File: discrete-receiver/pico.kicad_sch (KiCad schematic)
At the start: 49 parts, among them J4 Debug Pins, J8 Extra GPIO, U6 RP2350A, U7 W25Q128, X2 X322512MSB4SI

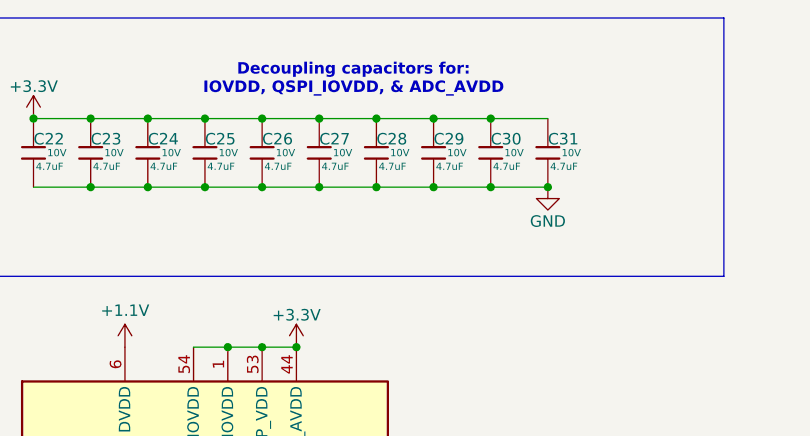
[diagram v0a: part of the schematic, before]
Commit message: Added test pads for SDA and SCL
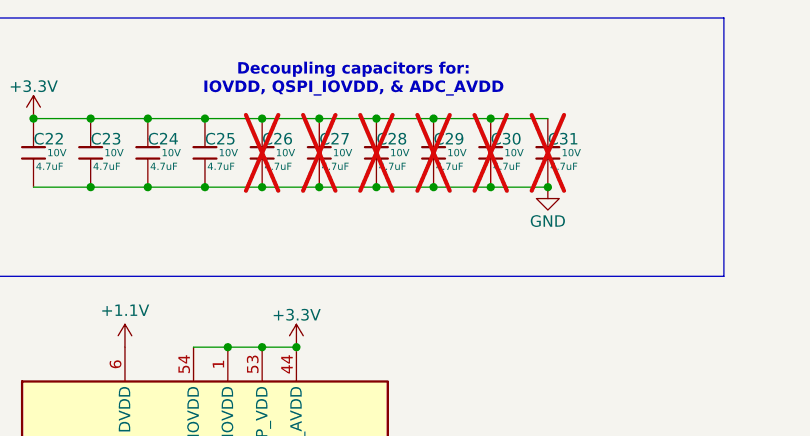
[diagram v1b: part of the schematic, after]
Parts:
- C26, C27, C28, C29, C30, C31: now not fitted; now left out of the parts list
- J8: footprint (none) -> Connector_PinHeader_2.54mm:PinHeader_1x05_P2.54mm_Vertical
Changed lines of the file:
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@@
 		(body_style 1)
 		(exclude_from_sim no)
-		(in_bom yes)
-		(on_board yes)
-		(in_pos_files yes)
-		(dnp no)
+		(in_bom no)
+		(on_board no)
+		(in_pos_files no)
+		(dnp yes)
 		(property "Reference" "C27"
 			(at 234.95 27.686 0)
@@
 		(body_style 1)
 		(exclude_from_sim no)
-		(in_bom yes)
-		(on_board yes)
-		(in_pos_files yes)
-		(dnp no)
+		(in_bom no)
+		(on_board no)
+		(in_pos_files no)
+		(dnp yes)
 		(property "Reference" "C28"
 			(at 241.3 27.686 0)
@@
 		(body_style 1)
 		(exclude_from_sim no)
-		(in_bom yes)
-		(on_board yes)
-		(in_pos_files yes)
-		(dnp no)
+		(in_bom no)
+		(on_board no)
+		(in_pos_files no)
+		(dnp yes)
 		(property "Reference" "C26"
 			(at 228.6 27.686 0)
@@
 			)
 		)
-		(property "Footprint" ""
+		(property "Footprint" "Connector_PinHeader_2.54mm:PinHeader_1x05_P2.54mm_Vertical"
 			(at 254 161.29 0)
 			(hide yes)
@@
 		(body_style 1)
 		(exclude_from_sim no)
-		(in_bom yes)
-		(on_board yes)
-		(in_pos_files yes)
-		(dnp no)
+		(in_bom no)
+		(on_board no)
+		(in_pos_files no)
+		(dnp yes)
 		(property "Reference" "C29"
 			(at 247.65 27.686 0)
@@
 		(body_style 1)
 		(exclude_from_sim no)
-		(in_bom yes)
-		(on_board yes)
-		(in_pos_files yes)
-		(dnp no)
+		(in_bom no)
+		(on_board no)
+		(in_pos_files no)
+		(dnp yes)
 		(property "Reference" "C30"
 			(at 254 27.686 0)
@@
 		(body_style 1)
 		(exclude_from_sim no)
-		(in_bom yes)
-		(on_board yes)
-		(in_pos_files yes)
-		(dnp no)
+		(in_bom no)
+		(on_board no)
+		(in_pos_files no)
+		(dnp yes)
 		(property "Reference" "C31"
 			(at 260.35 27.686 0)

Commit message: PCB Updates
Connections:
- net GND: now also J8.1 (Pin_1)
- net ~{ADC_RST}: now reaches U6.34 (GPIO22)
- net ~{ADC_RST}: no longer J8.1 (Pin_1)
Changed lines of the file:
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@@
 	(wire
 		(pts
+			(xy 259.08 153.67) (xy 259.08 156.21)
+		)
+		(stroke
+			(width 0)
+			(type default)
+		)
+	)
+	(wire
+		(pts
 			(xy 182.88 57.15) (xy 147.32 57.15)
 		)
@@
 	(wire
 		(pts
+			(xy 264.16 153.67) (xy 259.08 153.67)
+		)
+		(stroke
+			(width 0)
+			(type default)
+		)
+	)
+	(wire
+		(pts
 			(xy 147.32 52.07) (xy 147.32 57.15)
 		)
@@
 	(wire
 		(pts
-			(xy 259.08 156.21) (xy 259.08 130.81)
-		)
-		(stroke
-			(width 0)
-			(type default)
-		)
-	)
-	(wire
-		(pts
 			(xy 247.65 33.02) (xy 254 33.02)
 		)
@@
 	(wire
 		(pts
-			(xy 259.08 130.81) (xy 246.38 130.81)
-		)
-		(stroke
-			(width 0)
-			(type default)
-		)
-	)
-	(wire
-		(pts
 			(xy 147.32 52.07) (xy 147.32 49.53)
 		)
@@
 	(wire
 		(pts
+			(xy 264.16 156.21) (xy 264.16 153.67)
+		)
+		(stroke
+			(width 0)
+			(type default)
+		)
+	)
+	(wire
+		(pts
 			(xy 168.91 129.54) (xy 175.26 129.54)
 		)
@@
 		)
 	)
+	(hierarchical_label "~{ADC_RST}"
+		(shape input)
+		(at 246.38 130.81 0)
+		(effects
+			(font
+				(size 1.27 1.27)
+			)
+			(justify left)
+		)
+	)
 	(hierarchical_label "I2S_SCLK"
 		(shape input)
@@
 					(unit 1)
 				)
+			)
+		)
+	)
+	(symbol
+		(lib_id "power:GND")
+		(at 264.16 156.21 0)
+		(unit 1)
+		(body_style 1)
+		(exclude_from_sim no)
+		(in_bom yes)
+		(on_board yes)
+		(in_pos_files yes)
+		(dnp no)
+		(property "Reference" "#PWR020"
+			(at 264.16 162.56 0)
+			(hide yes)
+			(show_name no)
+			(do_not_autoplace no)
+			(effects
+				(font
+					(size 1.27 1.27)
+				)
+			)
+		)
+		(property "Value" "GND"
+			(at 264.16 159.766 0)
+			(show_name no)
+			(do_not_autoplace no)
+			(effects
+				(font
+					(size 1.27 1.27)
+				)
+			)
+		)
+		(property "Footprint" ""
+			(at 264.16 156.21 0)
+			(hide yes)
+			(show_name no)
+			(do_not_autoplace no)
+			(effects
+				(font
+					(size 1.27 1.27)
+				)
+			)
+		)
+		(property "Datasheet" ""
+			(at 264.16 156.21 0)
+			(hide yes)
+			(show_name no)
+			(do_not_autoplace no)
+			(effects
+				(font
+					(size 1.27 1.27)
+				)
+			)
+		)
+		(property "Description" "Power symbol creates a global label with name \"GND\" , ground"
+			(at 264.16 156.21 0)
+			(hide yes)
+			(show_name no)
+			(do_not_autoplace no)
+			(effects
+				(font
+					(size 1.27 1.27)
+				)
+			)
+		)
+		(pin "1"
+		)
+		(instances
+			(project "diode_tayloe_sdr"
+				(path "/d18d178d-3f10-4d68-9036-eae71a7d091a/55c641a1-b41f-4dd2-8726-b4449cdad787"
+					(reference "#PWR020")
+					(unit 1)
+				)

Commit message: Updated JLC part numbers because some parts were out of stock
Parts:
- U6: LCSC (none) -> C42411118
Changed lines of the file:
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@@
+			)
+		)
+		(property "LCSC" "C42411118"
+			(at 220.98 113.03 0)
+			(hide yes)
+			(show_name no)
+			(do_not_autoplace no)
+			(effects
+				(font
+					(size 1.27 1.27)
+				)
 			)
 		)

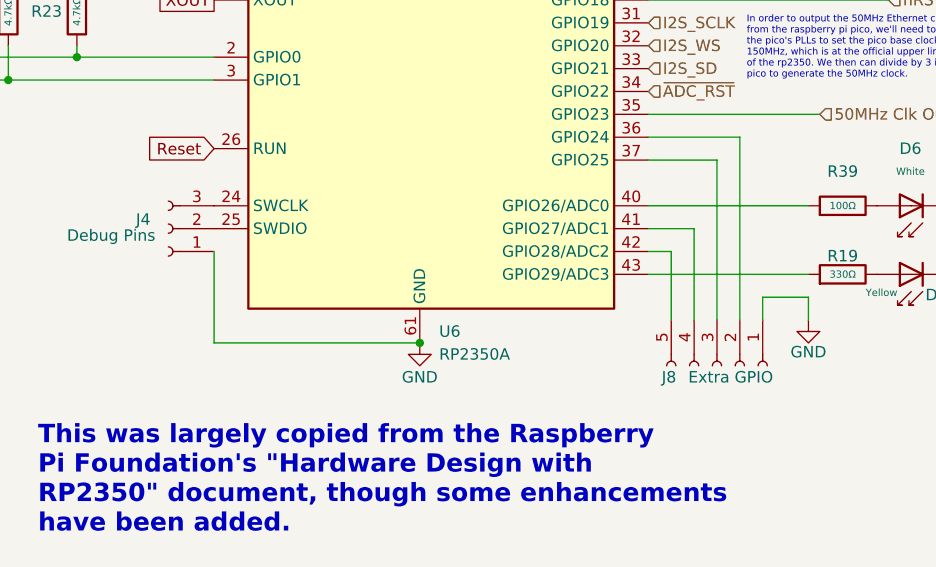
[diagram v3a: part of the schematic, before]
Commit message: Updated PCB DNP field for some parts
made pin headers and a few of the connectors DNP
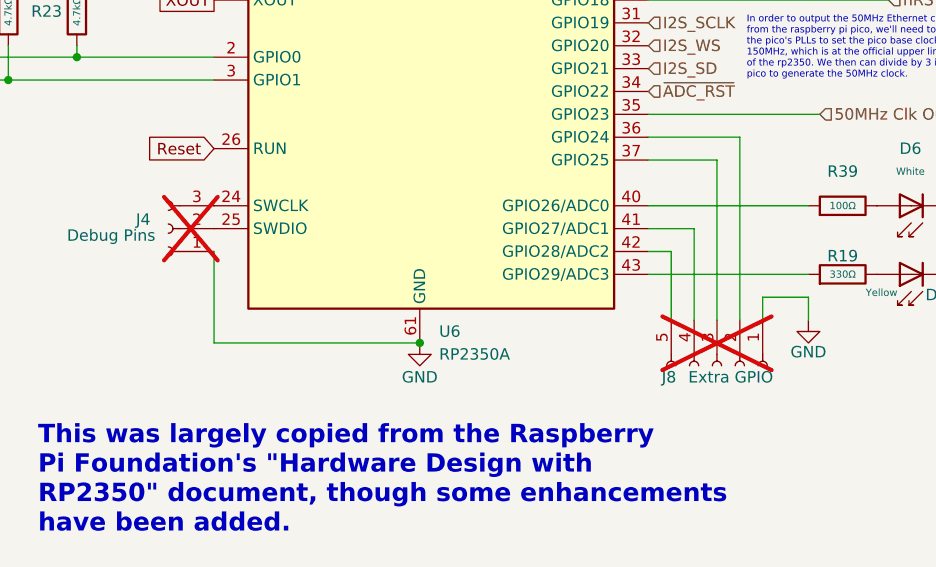
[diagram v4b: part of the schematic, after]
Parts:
- J4, J8: now not fitted; now left out of the parts list
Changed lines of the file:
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@@
 		(body_style 1)
 		(exclude_from_sim no)
-		(in_bom yes)
+		(in_bom no)
 		(on_board yes)
-		(in_pos_files yes)
-		(dnp no)
+		(in_pos_files no)
+		(dnp yes)
 		(property "Reference" "J4"
 			(at 190.246 145.034 0)
@@
 		(body_style 1)
 		(exclude_from_sim no)
-		(in_bom yes)
+		(in_bom no)
 		(on_board yes)
-		(in_pos_files yes)
-		(dnp no)
+		(in_pos_files no)
+		(dnp yes)
 		(property "Reference" "J8"
 			(at 248.666 162.56 90)

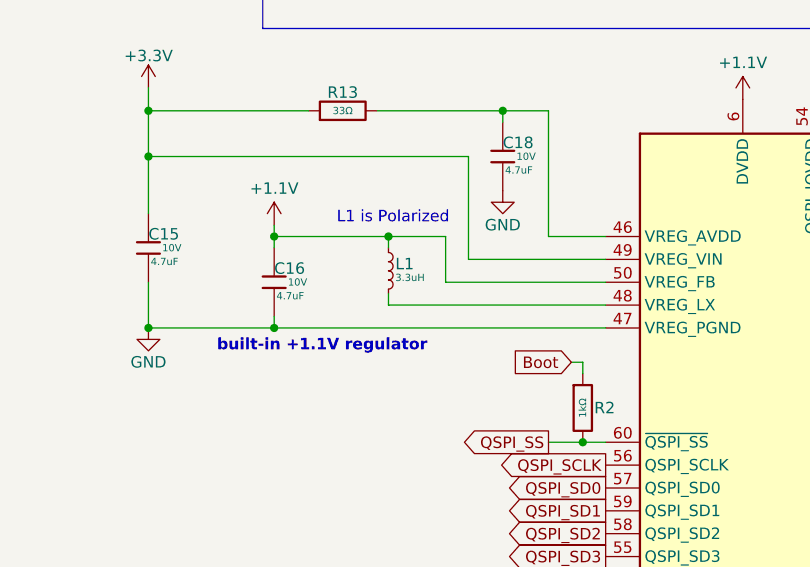
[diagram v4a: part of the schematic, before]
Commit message: replaced RJ45 connector 😡🙄🥀
The original was too expensive from JLCPCB and Digikey.
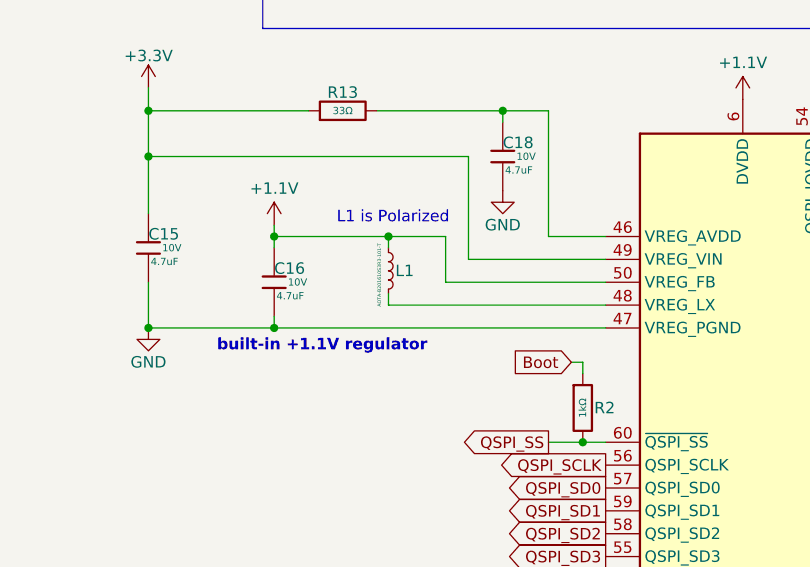
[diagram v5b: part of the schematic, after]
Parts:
- L1: value 3.3uH -> AOTA-B201610S3R3-101-T; LCSC (none) -> C42411119; LCSC Part Name 3.3uH 2.4A -> (none); Manufacturer Part AOTA-B201610S3R3-101-T -> (none); Supplier LCSC -> (none); Supplier Part C42411119 -> (none)
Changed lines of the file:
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@@
 		(dnp no)
 		(property "Reference" "L1"
-			(at 174.752 69.088 90)
+			(at 174.752 69.85 90)
 			(show_name no)
 			(do_not_autoplace no)
@@
 			)
 		)
-		(property "Value" "3.3uH"
-			(at 174.752 70.612 90)
+		(property "Value" "AOTA-B201610S3R3-101-T"
+			(at 172.974 66.802 0)
 			(show_name no)
 			(do_not_autoplace no)
 			(effects
 				(font
-					(size 0.8 0.8)
+					(size 0.381 0.381)
 				)
 				(justify left)
@@
 			)
 		)
-		(property "Manufacturer Part" "AOTA-B201610S3R3-101-T"
-			(at 173.99 69.85 0)
-			(hide yes)
-			(show_name no)
-			(do_not_autoplace no)
-			(effects
-				(font
-					(size 1.27 1.27)
-				)
-			)
-		)
 		(property "Manufacturer" "ABRACON"
 			(at 173.99 69.85 0)
@@
 			)
 		)
-		(property "Supplier Part" "C42411119"
+		(property "LCSC" "C42411119"
 			(at 173.99 69.85 0)
 			(hide yes)
-			(show_name no)
-			(do_not_autoplace no)
-			(effects
-				(font
-					(size 1.27 1.27)
-				)
-			)
-		)
-		(property "Supplier" "LCSC"
-			(at 173.99 69.85 0)
-			(hide yes)
-			(show_name no)
-			(do_not_autoplace no)
-			(effects
-				(font
-					(size 1.27 1.27)
-				)
-			)
-		)
-		(property "LCSC Part Name" "3.3uH 2.4A"
-			(at 173.99 69.85 0)
-			(hide yes)

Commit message: Fixed PCB component rotation offsets
A few components needed to get a rotation offset for JLCPCB production. Also more silkscreen content was added.
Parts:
- U6: Rotation Offset (none) -> 270
- U7: Rotation Offset (none) -> 90
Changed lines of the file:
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@@
 			)
 		)
+		(property "Rotation Offset" "90"
+			(at 57.15 167.64 0)
+			(hide yes)
+			(show_name no)
+			(do_not_autoplace no)
+			(effects
+				(font
+					(size 1.27 1.27)
+				)
+			)
+		)
 		(pin "4"
 		)
@@
 			(at 220.98 113.03 0)
 			(hide yes)
+			(show_name no)
+			(do_not_autoplace no)
+			(effects
+				(font
+					(size 1.27 1.27)
+				)
+			)
+		)
+		(property "Rotation Offset" "270"
+			(at 220.98 113.03 0)
+			(hide yes)
